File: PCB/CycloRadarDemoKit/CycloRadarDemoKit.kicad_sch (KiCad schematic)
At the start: 1 part, among them U101 ESP32-WROVER-E

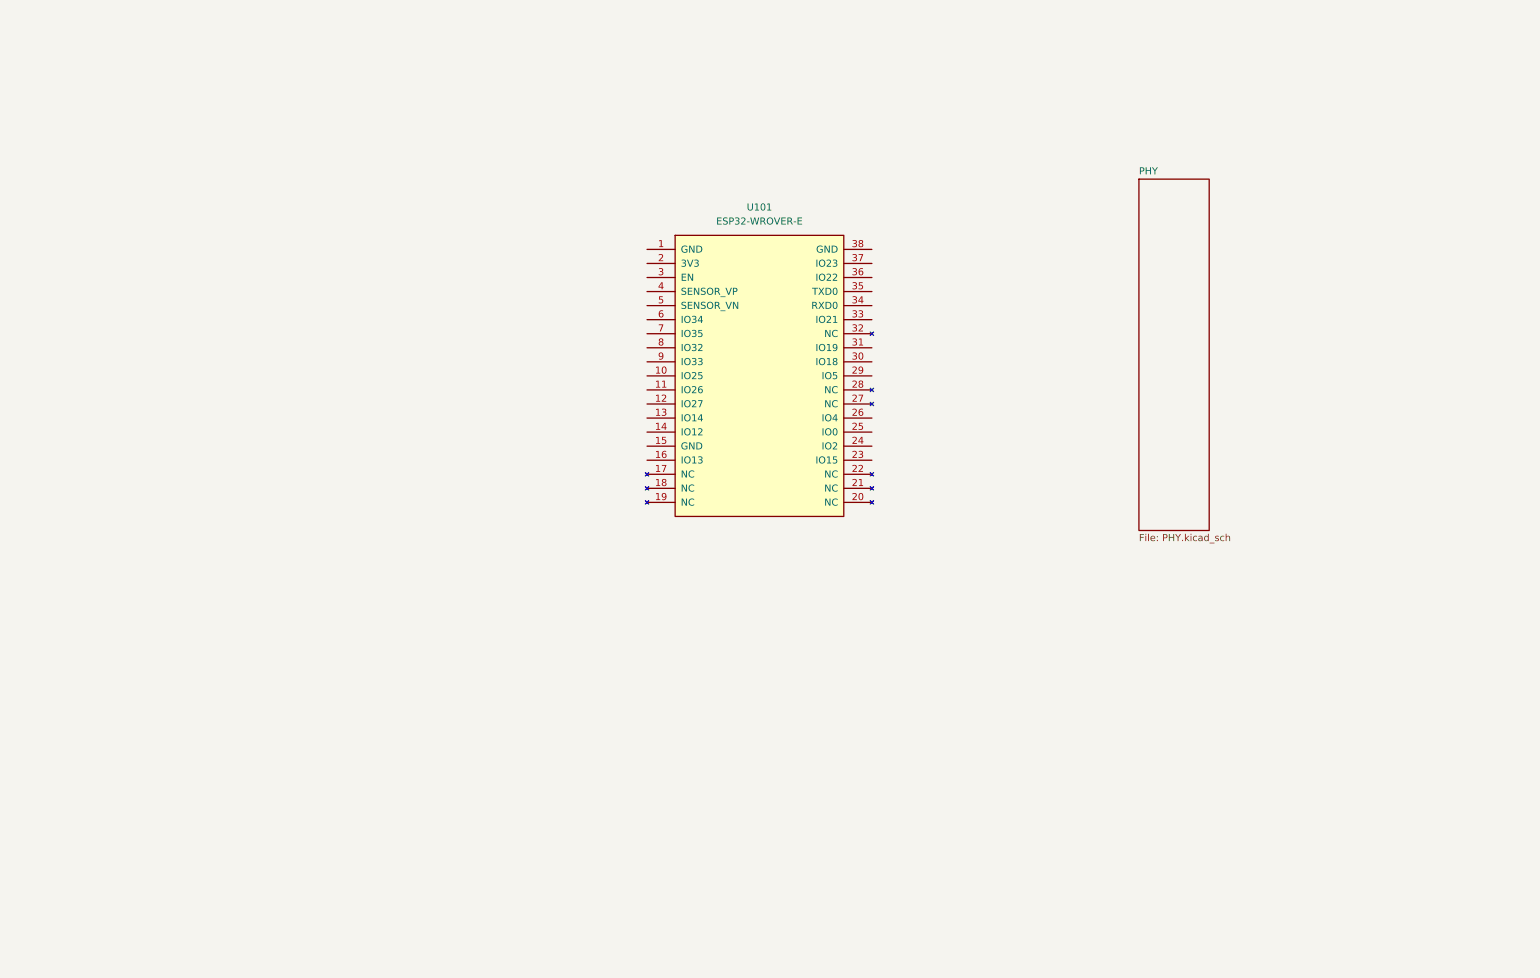
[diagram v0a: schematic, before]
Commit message: PCB WIP Started working on CP2102
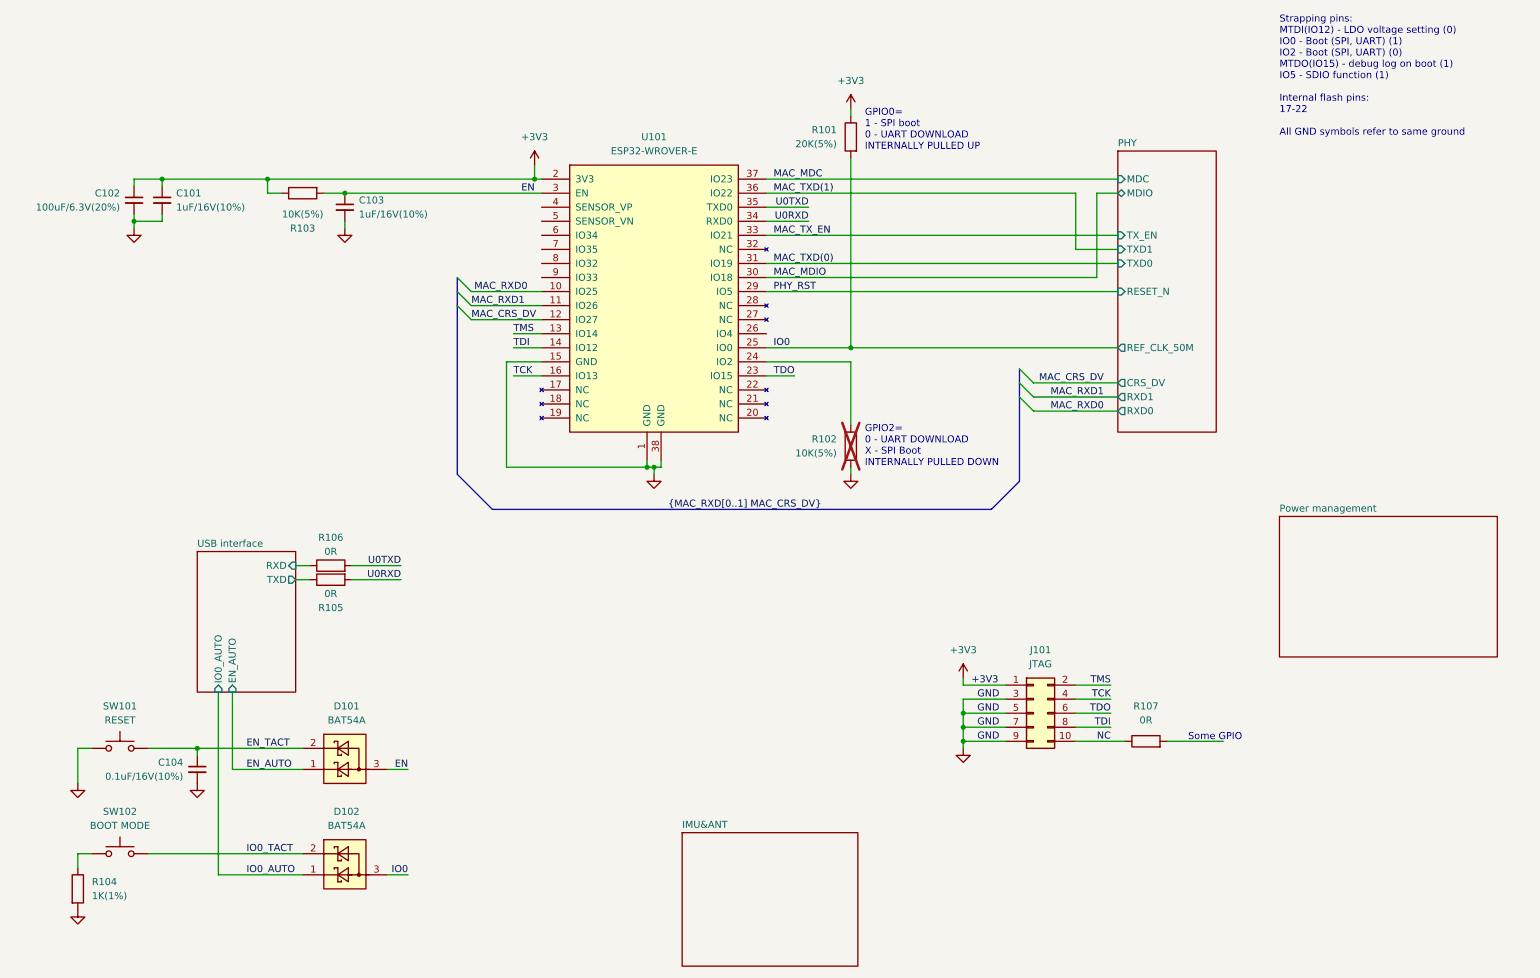
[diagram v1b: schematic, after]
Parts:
- added C101, C103: 1uF/16V(10%), symbol Device:C_Small
- added C102: 100uF/6.3V(20%), symbol Device:C_Small
- added C104: 0.1uF/16V(10%), symbol Device:C_Small
- added D101, D102: BAT54A, Package_TO_SOT_SMD:SOT-23, symbol Diode:BAT54A_edited
- added J101: JTAG, symbol Connector_Generic:Conn_02x05_Odd_Even
- added R101: 20K(5%), symbol Device:R
- added R102, R103: 10K(5%), symbol Device:R
- added R104: 1K(1%), symbol Device:R
- added R105, R106, R107: 0R, symbol Device:R
- added SW101: RESET, symbol Switch:SW_Push
- added SW102: BOOT MODE, symbol Switch:SW_Push
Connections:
- net GND: now reaches U101.1 (GND)
- net GND: now also U101.15 (GND), U101.38 (GND), C101.2, C102.2, C103.2, C104.2, J101.3 (Pin_3), J101.5 (Pin_5), J101.7 (Pin_7), J101.9 (Pin_9), R102.2, R104.2, SW101.1
- net MAC_RXD0: now reaches U101.10 (IO25)
- net MAC_RXD1: now reaches U101.11 (IO26)
- net MAC_CRS_DV: now reaches U101.12 (IO27)
- net TMS: now reaches U101.13 (IO14)
- net TMS: now also J101.2 (Pin_2)
- net TDI: now reaches U101.14 (IO12)
- net TDI: now also J101.8 (Pin_8)
- net TCK: now reaches U101.16 (IO13)
- net TCK: now also J101.4 (Pin_4)
- net +3V3: now reaches U101.2 (3V3)
- net +3V3: now also C101.1, C102.1, J101.1 (Pin_1), R101.1, R103.1
- net TDO: now reaches U101.23 (IO15)
- net TDO: now also J101.6 (Pin_6)
- net at U101.24 (IO2): now also R102.1
- net IO0: now reaches U101.25 (IO0)
- net IO0: now also D102.3, R101.2
- net PHY_RST: now reaches U101.29 (IO5)
- net EN: now reaches U101.3 (EN)
- net EN: now also C103.1, D101.3, R103.2
- net MAC_MDIO: now reaches U101.30 (IO18)
- net MAC_TXD(0): now reaches U101.31 (IO19)
- net MAC_TX_EN: now reaches U101.33 (IO21)
- net U0RXD: now reaches U101.34 (RXD0)
- net U0RXD: now also R105.2
- net U0TXD: now reaches U101.35 (TXD0)
- net U0TXD: now also R106.2
- net MAC_TXD(1): now reaches U101.36 (IO22)
- net MAC_MDC: now reaches U101.37 (IO23)
- new net: R104.1, SW102.1
- new net EN_AUTO: D101.1
- new net EN_TACT: C104.1, D101.2, SW101.2
- new net IO0_AUTO: D102.1
- new net IO0_TACT: D102.2, SW102.2
- new net NC: J101.10 (Pin_10), R107.1
- new net USB interface/RXD: R106.1
- new net USB interface/TXD: R105.1
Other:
- added sheet IMU&ANT (IMU&ANT.kicad_sch)
- added sheet Power management (PM.kicad_sch)
- added sheet USB interface (USB.kicad_sch)
- sheet PHY ports: added CRS_DV, MDC, MDIO, REF_CLK_50M, RESET_N, RXD0, RXD1, TXD0, TXD1, TX_EN; removed none
- note added: "GPIO0= 1 - SPI boot 0 - UART DOWNLOAD INTERNALLY PULLED UP"
- note added: "GPIO2= 0 - UART DOWNLOAD X - SPI Boot INTERNALLY PULLED DOWN"
- note added: "Some GPIO"
- note added: "Strapping pins: MTDI(IO12) - LDO voltage setting (0) IO0 - Boot (SPI, UART) (1) IO2 - Boot (SPI, UART) (0) MTDO(IO15) - debug log on boot (1) IO5 - SDIO function (1) Internal flash pins: 17-22 All GND symbols refer to same ground"
- company: (none) -> Alps Electric Czech, s.r.o.
- title: (none) -> Development module for Radar Safety Sensor
- moved on the sheet: U101

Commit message: USB designed with TODOs, ESP part changed
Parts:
- U101: footprint EspressIf:ESP32-WROVER-IE -> Espressif:ESP32-WROVER-E_ThermalVias
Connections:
- net +3V3: no longer U101.2 (3V3)
- net EN: no longer U101.3 (EN)
- net GND: no longer U101.1 (GND), U101.15 (GND), U101.38 (GND)
- net IO0: no longer U101.25 (IO0)
- net MAC_CRS_DV: no longer U101.12 (IO27)
- net MAC_MDC: no longer U101.37 (IO23)
- net MAC_MDIO: no longer U101.30 (IO18)
- net MAC_RXD0: no longer U101.10 (IO25)
- net MAC_RXD1: no longer U101.11 (IO26)
- net MAC_TXD(0): no longer U101.31 (IO19)
- net MAC_TXD(1): no longer U101.36 (IO22)
- net MAC_TX_EN: no longer U101.33 (IO21)
- net PHY_RST: no longer U101.29 (IO5)
- net TCK: no longer U101.16 (IO13)
- net TDI: no longer U101.14 (IO12)
- net TDO: no longer U101.23 (IO15)
- net TMS: no longer U101.13 (IO14)
- net U0RXD: no longer U101.34 (RXD0)
- net U0TXD: no longer U101.35 (TXD0)
- net at R102.1: no longer U101.24 (IO2)
- new net: U101.1 (GND), U101.15 (GND), U101.38 (GND)
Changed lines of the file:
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@@
     )
   )
-  (symbol (lib_id "power:GND") (at 184.15 151.13 0) (unit 1)
-    (in_bom yes) (on_board yes) (dnp no) (fields_autoplaced)
-    (property "Reference" "#PWR0110" (at 184.15 157.48 0)
-      (effects (font (size 1.27 1.27)) hide)
-    )
-    (property "Value" "GND" (at 184.15 156.21 0)
-      (effects (font (size 1.27 1.27)) hide)
-    )
-    (property "Footprint" "" (at 184.15 151.13 0)
-      (effects (font (size 1.27 1.27)) hide)
-    )
-    (property "Datasheet" "" (at 184.15 151.13 0)
-      (effects (font (size 1.27 1.27)) hide)
-    )
-    (pin "1")
-    (instances
-      (project "CycloRadarDemoKit"
-        (path "/c2cd7ca4-4652-4b3d-a3a8-1cfa66cb11e9"
-          (reference "#PWR0110") (unit 1)
-        )
-      )
-    )
-  )
-  (symbol (lib_id "power:GND") (at 128.27 101.6 0) (unit 1)
-    (in_bom yes) (on_board yes) (dnp no) (fields_autoplaced)
-    (property "Reference" "#PWR0106" (at 128.27 107.95 0)
-      (effects (font (size 1.27 1.27)) hide)
-    )
-    (property "Value" "GND" (at 128.27 106.68 0)
-      (effects (font (size 1.27 1.27)) hide)
-    )
-    (property "Footprint" "" (at 128.27 101.6 0)
-      (effects (font (size 1.27 1.27)) hide)
-    )
-    (property "Datasheet" "" (at 128.27 101.6 0)
-      (effects (font (size 1.27 1.27)) hide)
-    )
-    (pin "1")
-    (instances
-      (project "CycloRadarDemoKit"
-        (path "/c2cd7ca4-4652-4b3d-a3a8-1cfa66cb11e9"
-          (reference "#PWR0106") (unit 1)
-        )
-      )
-    )
-  )
-  (symbol (lib_id "power:+3V3") (at 163.83 35.56 0) (unit 1)
-    (in_bom yes) (on_board yes) (dnp no) (fields_autoplaced)
-    (property "Reference" "#PWR0101" (at 163.83 39.37 0)
-      (effects (font (size 1.27 1.27)) hide)
-    )
-    (property "Value" "+3V3" (at 163.83 30.48 0)
-      (effects (font (size 1.27 1.27)))
-    )
-    (property "Footprint" "" (at 163.83 35.56 0)
-      (effects (font (size 1.27 1.27)) hide)
-    )
-    (property "Datasheet" "" (at 163.83 35.56 0)
-      (effects (font (size 1.27 1.27)) hide)
-    )
-    (pin "1")
-    (instances
-      (project "CycloRadarDemoKit"
-        (path "/c2cd7ca4-4652-4b3d-a3a8-1cfa66cb11e9"
-          (reference "#PWR0101") (unit 1)
-        )
-      )
-    )
-  )
-  (symbol (lib_id "power:GND") (at 163.83 101.6 0) (unit 1)
-    (in_bom yes) (on_board yes) (dnp no) (fields_autoplaced)
-    (property "Reference" "#PWR0102" (at 163.83 107.95 0)
-      (effects (font (size 1.27 1.27)) hide)
-    )
-    (property "Value" "GND" (at 163.83 106.68 0)
-      (effects (font (size 1.27 1.27)) hide)
-    )
-    (property "Footprint" "" (at 163.83 101.6 0)
-      (effects (font (size 1.27 1.27)) hide)
-    )
-    (property "Datasheet" "" (at 163.83 101.6 0)
-      (effects (font (size 1.27 1.27)) hide)
-    )
-    (pin "1")
-    (instances
-      (project "CycloRadarDemoKit"
-        (path "/c2cd7ca4-4652-4b3d-a3a8-1cfa66cb11e9"
-          (reference "#PWR0102") (unit 1)
-        )
-      )
-    )
-  )
-  (symbol (lib_id "EspressIf:ESP32-WROVER-E") (at 128.27 68.58 0) (unit 1)
-    (in_bom yes) (on_board yes) (dnp no) (fields_autoplaced)
-    (property "Reference" "U101" (at 128.27 40.64 0)
-      (effects (font (size 1.27 1.27)))
-    )
-    (property "Value" "ESP32-WROVER-E" (at 128.27 43.18 0)
-      (effects (font (size 1.27 1.27)))
-    )
-    (property "Footprint" "EspressIf:ESP32-WROVER-IE" (at 128.27 59.69 0)
-      (effects (font (size 1.27 1.27)) hide)
-    )
-    (property "Datasheet" "" (at 128.27 59.69 0)
-      (effects (font (size 1.27 1.27)) hide)
-    )
-    (pin "19")
-    (pin "17")
+  (symbol (lib_id "EspressIf:ESP32-WROVER-E") (at 130.81 138.43 0) (unit 1)
+    (in_bom yes) (on_board yes) (dnp no) (fields_autoplaced)
+    (property "Reference" "U101" (at 133.0041 113.03 0)
+      (effects (font (size 1.27 1.27)) (justify left))
+    )
+    (property "Value" "ESP32-WROVER-E" (at 133.0041 115.57 0)
+      (effects (font (size 1.27 1.27)) (justify left))
+    )
+    (property "Footprint" "Espressif:ESP32-WROVER-E_ThermalVias" (at 133.35 171.45 0)
+      (effects (font (size 1.27 1.27)) hide)
+    )
+    (property "Datasheet" "https://www.espressif.com/sites/default/files/documentation/esp32-wrover-e_esp32-wrover-ie_datasheet_en.pdf" (at 133.35 173.99 0)
+      (effects (font (size 1.27 1.27)) hide)
+    )
+    (pin "4")
+    (pin "34")
+    (pin "36")
+    (pin "29")
+    (pin "37")
+    (pin "38")
+    (pin "9")
+    (pin "6")
+    (pin "30")
     (pin "25")
     (pin "31")
-    (pin "37")
-    (pin "38")
-    (pin "32")
-    (pin "20")
     (pin "35")
+    (pin "7")
+    (pin "3")
+    (pin "39")
+    (pin "24")
     (pin "26")
-    (pin "7")
-    (pin "21")
-    (pin "3")
     (pin "8")
-    (pin "22")
     (pin "5")
-    (pin "9")
-    (pin "1")
+    (pin "33")
+    (pin "11")
+    (pin "12")
+    (pin "13")
+    (pin "23")
+    (pin "10")
+    (pin "1")
+    (pin "15")
     (pin "14")
-    (pin "27")
-    (pin "29")
-    (pin "33")
-    (pin "28")
-    (pin "11")
-    (pin "15")
-    (pin "18")
-    (pin "13")
-    (pin "2")
-    (pin "24")
-    (pin "10")
-    (pin "12")
-    (pin "30")
-    (pin "34")
-    (pin "36")
-    (pin "23")
-    (pin "4")
-    (pin "6")
     (pin "16")
+    (pin "2")
     (instances
       (project "CycloRadarDemoKit"
@@
           (reference "U101") (unit 1)
         )
-        (path "/c2cd7ca4-4652-4b3d-a3a8-1cfa66cb11e9/8ae18a6c-482d-4e1c-94d1-12de0ef4fa68"
-          (reference "U1") (unit 1)
+      )
+    )
+  )
+  (symbol (lib_id "power:GND") (at 184.15 151.13 0) (unit 1)
+    (in_bom yes) (on_board yes) (dnp no) (fields_autoplaced)
+    (property "Reference" "#PWR0110" (at 184.15 157.48 0)
+      (effects (font (size 1.27 1.27)) hide)
+    )
+    (property "Value" "GND" (at 184.15 156.21 0)
+      (effects (font (size 1.27 1.27)) hide)
+    )
+    (property "Footprint" "" (at 184.15 151.13 0)
+      (effects (font (size 1.27 1.27)) hide)
+    )
+    (property "Datasheet" "" (at 184.15 151.13 0)
+      (effects (font (size 1.27 1.27)) hide)
+    )
+    (pin "1")
+    (instances
+      (project "CycloRadarDemoKit"
+        (path "/c2cd7ca4-4652-4b3d-a3a8-1cfa66cb11e9"
+          (reference "#PWR0110") (unit 1)
+        )
+      )
+    )
+  )
+  (symbol (lib_id "power:GND") (at 128.27 101.6 0) (unit 1)
+    (in_bom yes) (on_board yes) (dnp no) (fields_autoplaced)
+    (property "Reference" "#PWR0106" (at 128.27 107.95 0)
+      (effects (font (size 1.27 1.27)) hide)
+    )
+    (property "Value" "GND" (at 128.27 106.68 0)
+      (effects (font (size 1.27 1.27)) hide)
+    )
+    (property "Footprint" "" (at 128.27 101.6 0)
+      (effects (font (size 1.27 1.27)) hide)
+    )
+    (property "Datasheet" "" (at 128.27 101.6 0)
+      (effects (font (size 1.27 1.27)) hide)
+    )
+    (pin "1")
+    (instances
+      (project "CycloRadarDemoKit"
+        (path "/c2cd7ca4-4652-4b3d-a3a8-1cfa66cb11e9"
+          (reference "#PWR0106") (unit 1)
+        )
+      )
+    )
+  )
+  (symbol (lib_id "power:+3V3") (at 163.83 35.56 0) (unit 1)
+    (in_bom yes) (on_board yes) (dnp no) (fields_autoplaced)
+    (property "Reference" "#PWR0101" (at 163.83 39.37 0)
+      (effects (font (size 1.27 1.27)) hide)
+    )
+    (property "Value" "+3V3" (at 163.83 30.48 0)
+      (effects (font (size 1.27 1.27)))
+    )
+    (property "Footprint" "" (at 163.83 35.56 0)
+      (effects (font (size 1.27 1.27)) hide)
+    )
+    (property "Datasheet" "" (at 163.83 35.56 0)
+      (effects (font (size 1.27 1.27)) hide)
+    )
+    (pin "1")
+    (instances
+      (project "CycloRadarDemoKit"
+        (path "/c2cd7ca4-4652-4b3d-a3a8-1cfa66cb11e9"
+          (reference "#PWR0101") (unit 1)
+        )
+      )
+    )
+  )
+  (symbol (lib_id "power:GND") (at 163.83 101.6 0) (unit 1)
+    (in_bom yes) (on_board yes) (dnp no) (fields_autoplaced)
+    (property "Reference" "#PWR0102" (at 163.83 107.95 0)
+      (effects (font (size 1.27 1.27)) hide)
+    )
+    (property "Value" "GND" (at 163.83 106.68 0)
+      (effects (font (size 1.27 1.27)) hide)
+    )
+    (property "Footprint" "" (at 163.83 101.6 0)
+      (effects (font (size 1.27 1.27)) hide)
+    )
+    (property "Datasheet" "" (at 163.83 101.6 0)
+      (effects (font (size 1.27 1.27)) hide)
+    )
+    (pin "1")
+    (instances
+      (project "CycloRadarDemoKit"
+        (path "/c2cd7ca4-4652-4b3d-a3a8-1cfa66cb11e9"
+          (reference "#PWR0102") (unit 1)
         )
       )
@@
       (effects (font (size 1.27 1.27)) hide)
     )
-    (pin "EN_AUTO" input (at 52.07 140.97 270)
-      (effects (font (size 1.27 1.27)) (justify left))
-    )
-    (pin "IO0_AUTO" input (at 49.53 140.97 270)
-      (effects (font (size 1.27 1.27)) (justify left))
-    )
+    (pin "EN_AUTO" output (at 52.07 140.97 270)
+      (effects (font (size 1.27 1.27)) (justify left))
+    )
+    (pin "IO0_AUTO" output (at 49.53 140.97 270)
+      (effects (font (size 1.27 1.27)) (justify left))
+    )
